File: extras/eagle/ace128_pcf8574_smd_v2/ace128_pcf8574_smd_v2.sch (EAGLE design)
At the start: 13 parts, among them J1 GROVE I2C, U1 PCF8574T

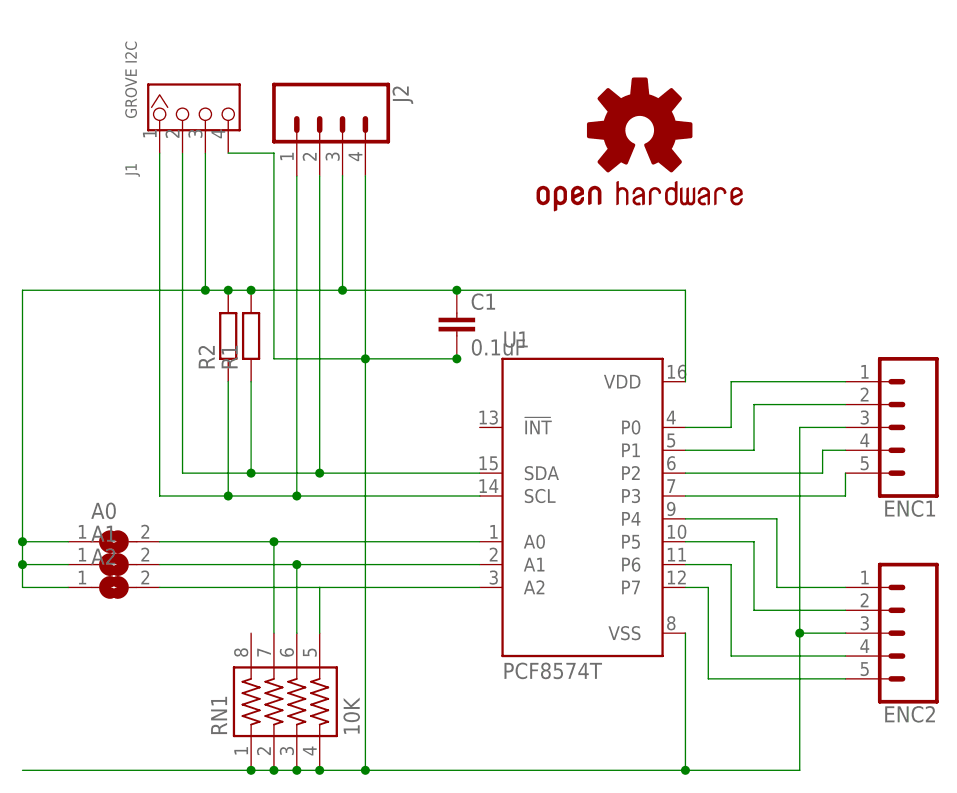
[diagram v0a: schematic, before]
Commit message: v2.1 board
change c1 to 0603
add c2 10uf 0805
route tidying
silkscreen adds for version and address ranges.
general silkscreen shuffle
tented vias
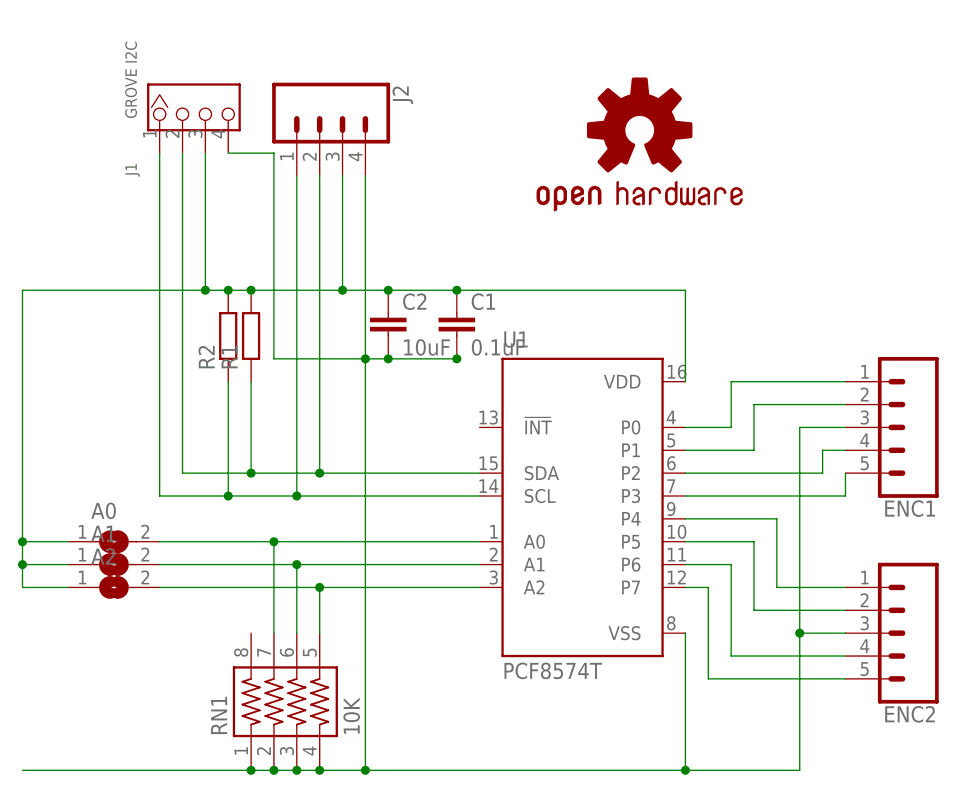
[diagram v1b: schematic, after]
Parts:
- added C2: 10uF, rcl:C-EUC0805
- C1: device rcl:C-EUC0805 -> rcl:C-EUC0603
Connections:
- net GND: now also C2.2
- net VCC: now also C2.1
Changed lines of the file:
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@@
 <?xml version="1.0" encoding="utf-8"?>
 <!DOCTYPE eagle SYSTEM "eagle.dtd">
-<eagle version="7.7.0">
+<eagle version="8.4.2">
 <drawing>
 <settings>
 <setting alwaysvectorfont="no"/>
+<setting keepoldvectorfont="yes"/>
 <setting verticaltext="up"/>
 </settings>
@@
 <part name="U1" library="micro-philips" deviceset="PCF8574" device="T" value="PCF8574T"/>
 <part name="J2" library="SparkFun-Connectors" deviceset="CONN_04" device=""/>
-<part name="C1" library="rcl" deviceset="C-EU" device="C0805" value="0.1uF"/>
+<part name="C1" library="rcl" library_urn="urn:adsk.eagle:library:334" deviceset="C-EU" device="C0603" package3d_urn="urn:adsk.eagle:package:23616/2" value="0.1uF"/>
 <part name="J1" library="Seeed-OPL-Connector" deviceset="GROVE-CONNECTOR-DIP(4P-2.0)" device="" value="GROVE I2C"/>
 <part name="R1" library="rcl" deviceset="R-EU_" device="0207/2V"/>
@@
 <part name="A2" library="jumper" deviceset="SJ" device=""/>
 <part name="LOGO1" library="SparkFun-Aesthetics" deviceset="OSHW-LOGO" device="S"/>
+<part name="C2" library="rcl" deviceset="C-EU" device="C0805" value="10uF"/>
 </parts>
 <sheets>
@@
 <instance part="A2" gate="1" x="25.4" y="35.56"/>
 <instance part="LOGO1" gate="G$1" x="83.82" y="86.36"/>
+<instance part="C2" gate="G$1" x="55.88" y="66.04"/>
 </instances>
 <busses>
@@
 <wire x1="88.9" y1="30.48" x2="88.9" y2="15.24" width="0.1524" layer="91"/>
 <pinref part="C1" gate="G$1" pin="2"/>
-<wire x1="53.34" y1="60.96" x2="63.5" y2="60.96" width="0.1524" layer="91"/>
+<wire x1="53.34" y1="60.96" x2="55.88" y2="60.96" width="0.1524" layer="91"/>
 <pinref part="J2" gate="G$1" pin="4"/>
+<wire x1="55.88" y1="60.96" x2="63.5" y2="60.96" width="0.1524" layer="91"/>
 <wire x1="53.34" y1="81.28" x2="53.34" y2="60.96" width="0.1524" layer="91"/>
 <junction x="53.34" y="60.96"/>
@@
 <pinref part="RN1" gate="G$1" pin="4"/>
 <junction x="48.26" y="15.24"/>
+<pinref part="C2" gate="G$1" pin="2"/>
+<junction x="55.88" y="60.96"/>
 </segment>
 </net>
 <net name="VCC" class="0">
 <segment>
-<wire x1="63.5" y1="68.58" x2="50.8" y2="68.58" width="0.1524" layer="91"/>
+<wire x1="63.5" y1="68.58" x2="55.88" y2="68.58" width="0.1524" layer="91"/>
 <pinref part="U1" gate="G$1" pin="VDD"/>
+<wire x1="55.88" y1="68.58" x2="50.8" y2="68.58" width="0.1524" layer="91"/>
 <wire x1="50.8" y1="68.58" x2="40.64" y2="68.58" width="0.1524" layer="91"/>
 <wire x1="40.64" y1="68.58" x2="38.1" y2="68.58" width="0.1524" layer="91"/>
@@
 <junction x="15.24" y="40.64"/>
 <junction x="15.24" y="38.1"/>
+<pinref part="C2" gate="G$1" pin="1"/>
+<junction x="55.88" y="68.58"/>
 </segment>
 </net>
@@
 <wire x1="48.26" y1="35.56" x2="30.48" y2="35.56" width="0.1524" layer="91"/>
 <wire x1="48.26" y1="30.48" x2="48.26" y2="35.56" width="0.1524" layer="91"/>
+<junction x="48.26" y="35.56"/>
 </segment>
 </net>
@@
 </schematic>
 </drawing>
+<compatibility>
+<note version="8.2" severity="warning">
+Since Version 8.2, EAGLE supports online libraries. The ids
+of those online libraries will not be understood (or retained)
+with this version.
+</note>
+<note version="8.3" severity="warning">
+Since Version 8.3, EAGLE supports URNs for individual library
+assets (packages, symbols, and devices). The URNs of those assets
+will not be understood (or retained) with this version.
+</note>
+<note version="8.3" severity="warning">
+Since Version 8.3, EAGLE supports the association of 3D packages
+with devices in libraries, schematics, and board files. Those 3D
+packages will not be understood (or retained) with this version.
+</note>
+</compatibility>
 </eagle>
